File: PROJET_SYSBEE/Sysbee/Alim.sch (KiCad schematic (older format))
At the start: 11 parts, among them U2 LT1764, U3 AP1117-33

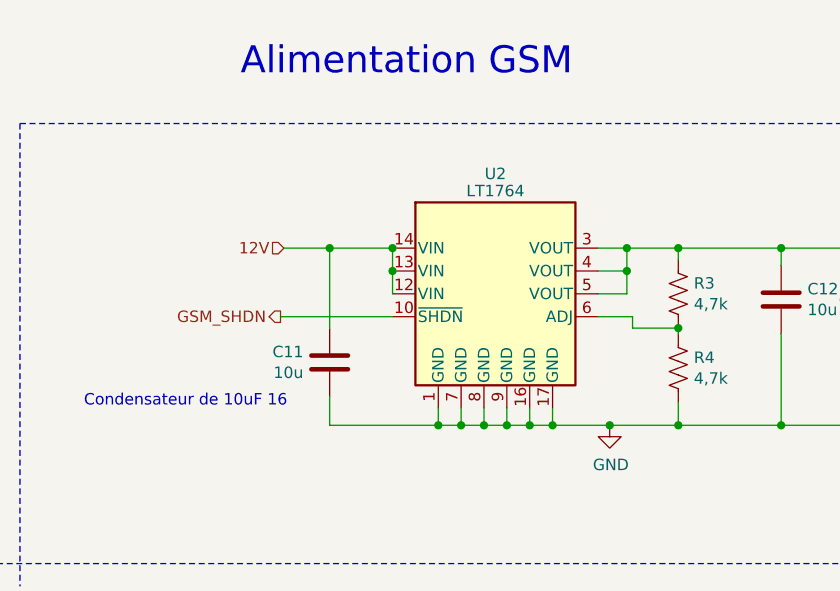
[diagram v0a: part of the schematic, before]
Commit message: placement et routage, reste à redessiner un peu les pistes et rajouter les écritures F.Silks
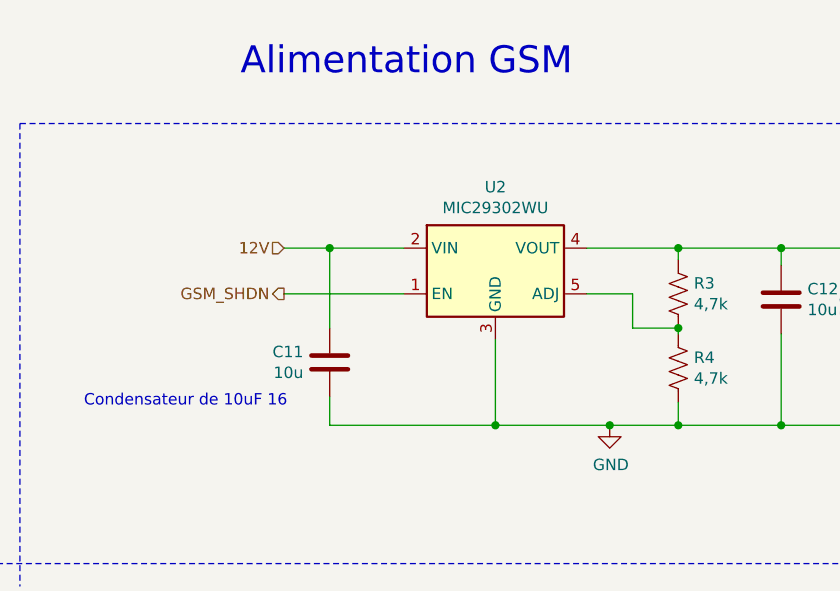
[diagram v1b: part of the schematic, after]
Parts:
- removed U2: LT1764, Package_SO:HTSSOP-16-1EP_4.4x5mm_P0.65mm_EP3.4x5mm_Mask3x3mm_ThermalVias, symbol sysbee:LT1764
- added U2: MIC29302WU, Package_TO_SOT_SMD:TO-263-5_TabPin3, symbol Regulator_Linear:MIC29302WU
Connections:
- net 12V: now also U2.2 (VIN)
- net 3,9V: now also U2.4 (VOUT)
- net GND: now also U2.3 (GND)
- net GSM_SHDN: now also U2.1 (EN)
- net at R3.2, R4.1: now also U2.5 (ADJ)
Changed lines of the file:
@@
 Wire Wire Line
 	4575 4200 4775 4200
-Text HLabel 4560 4500 0    50   Output ~ 0
+Text HLabel 4575 4400 0    50   Output ~ 0
 GSM_SHDN
-Wire Wire Line
-	5050 4500 4560 4500
 $Comp
 L Sysbee-rescue:AP1117-33-Regulator_Linear U?
@@
 	0    1    1    0
 $EndComp
-Connection ~ 5050 4200
-Wire Wire Line
-	5050 4200 5050 4300
-Wire Wire Line
-	5050 4300 5050 4400
-Connection ~ 5050 4300
-$Comp
-L sysbee:LT1764 U2
-U 1 1 6046F3AF
-P 5450 4200
-F 0 "U2" H 5500 4525 50  0000 C CNN
-F 1 "LT1764" H 5500 4450 50  0000 C CNN
-F 2 "Package_SO:HTSSOP-16-1EP_4.4x5mm_P0.65mm_EP3.4x5mm_Mask3x3mm_ThermalVias" H 5050 4750 50  0001 C CNN
-F 3 "https://www.analog.com/media/en/technical-documentation/data-sheets/1761sff.pdf" H 5450 4200 50  0001 C CNN
-	1    5450 4200
-	1    0    0    -1
-$EndComp
-Wire Wire Line
-	5250 4900 5250 4975
-Wire Wire Line
-	5250 4975 5350 4975
 Wire Wire Line
 	6750 4975 6750 4575
@@
 $EndComp
 Wire Wire Line
-	5950 4500 6100 4500
-Wire Wire Line
-	6100 4500 6100 4550
-Wire Wire Line
 	6100 4550 6300 4550
 Wire Wire Line
 	6300 4250 6300 4200
-Wire Wire Line
-	5950 4200 6075 4200
 Wire Wire Line
 	6300 4200 6750 4200
@@
 Connection ~ 4775 4200
 Wire Wire Line
-	4775 4200 5050 4200
-Wire Wire Line
 	4775 4850 4775 4975
 Wire Wire Line
-	4775 4975 5250 4975
-Connection ~ 5250 4975
-Connection ~ 6000 4975
-Wire Wire Line
 	6000 4975 6300 4975
-Wire Wire Line
-	5350 4900 5350 4975
-Connection ~ 5350 4975
-Wire Wire Line
-	5350 4975 5450 4975
-Wire Wire Line
-	5450 4900 5450 4975
-Connection ~ 5450 4975
-Wire Wire Line
-	5450 4975 5550 4975
-Wire Wire Line
-	5550 4900 5550 4975
-Connection ~ 5550 4975
-Wire Wire Line
-	5550 4975 5650 4975
-Wire Wire Line
-	5650 4900 5650 4975
-Connection ~ 5650 4975
-Wire Wire Line
-	5650 4975 5750 4975
-Wire Wire Line
-	5750 4900 5750 4975
-Connection ~ 5750 4975
-Wire Wire Line
-	5750 4975 6000 4975
-Wire Wire Line
-	5950 4300 6075 4300
-Wire Wire Line
-	6075 4300 6075 4200
-Connection ~ 6075 4200
-Wire Wire Line
-	6075 4200 6300 4200
-Wire Wire Line
-	5950 4400 6075 4400
-Wire Wire Line
-	6075 4400 6075 4300
-Connection ~ 6075 4300
 Text Notes 3700 4900 0    50   ~ 0
 Condensateur de 10uF 16
@@
 Text Notes 4900 2500 0    50   ~ 0
 Condensateur de 47uF 16V\n
+$Comp
+L Regulator_Linear:MIC29302WU U2
+U 1 1 6048195D
+P 5500 4300
+F 0 "U2" H 5500 4667 50  0000 C CNN
+F 1 "MIC29302WU" H 5500 4576 50  0000 C CNN
+F 2 "Package_TO_SOT_SMD:TO-263-5_TabPin3" H 5600 4050 50  0001 L CNN
+F 3 "http://ww1.microchip.com/downloads/en/devicedoc/20005685a.pdf" H 5500 4300 50  0001 C CNN
+	1    5500 4300
+	1    0    0    -1
+$EndComp
+Wire Wire Line
+	6100 4400 5900 4400
+Wire Wire Line
+	6100 4400 6100 4550
+Wire Wire Line
+	5900 4200 6300 4200
+Wire Wire Line
+	4775 4200 5100 4200
+Wire Wire Line
+	4575 4400 5100 4400
+Connection ~ 6000 4975
+Wire Wire Line
+	5500 4600 5500 4975
+Wire Wire Line
+	4775 4975 5500 4975
+Connection ~ 5500 4975
+Wire Wire Line
+	5500 4975 6000 4975
 $EndSCHEMATC

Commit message: placement et routage ok
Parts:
- R3: value 4,7k -> 430
- R4: value 4,7k -> 200
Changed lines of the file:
@@
 Wire Wire Line
 	4575 4200 4775 4200
-Text HLabel 4575 4400 0    50   Output ~ 0
+Text HLabel 4575 4400 0    50   Input ~ 0
 GSM_SHDN
 $Comp
@@
 P 6300 4400
 F 0 "R3" H 6368 4446 50  0000 L CNN
-F 1 "4,7k" H 6368 4355 50  0000 L CNN
+F 1 "430" H 6368 4355 50  0000 L CNN
 F 2 "Resistor_SMD:R_1206_3216Metric" V 6340 4390 50  0001 C CNN
 F 3 "~" H 6300 4400 50  0001 C CNN
@@
 P 6300 4725
 F 0 "R4" H 6368 4771 50  0000 L CNN
-F 1 "4,7k" H 6368 4680 50  0000 L CNN
+F 1 "200" H 6368 4680 50  0000 L CNN
 F 2 "Resistor_SMD:R_1206_3216Metric" V 6340 4715 50  0001 C CNN
 F 3 "~" H 6300 4725 50  0001 C CNN
